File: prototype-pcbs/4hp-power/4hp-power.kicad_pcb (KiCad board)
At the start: 2 copper layers, 17.8 x 109.2 mm, 208 parts, among them J1 IDC Header 2x8

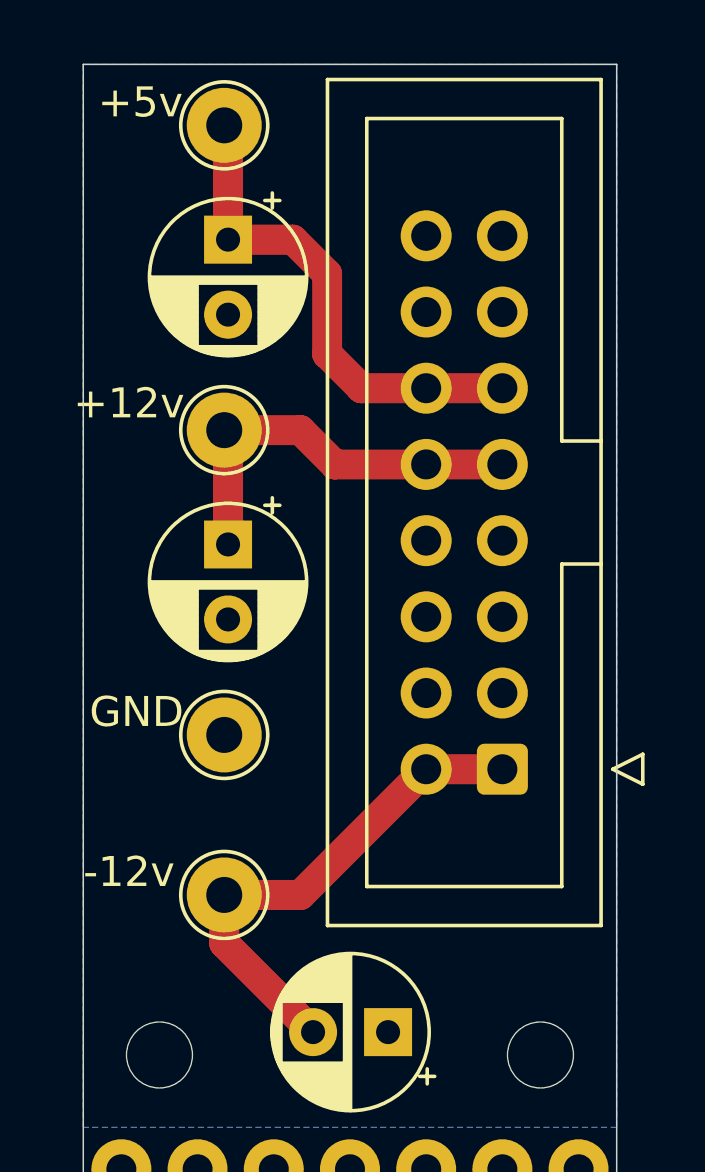
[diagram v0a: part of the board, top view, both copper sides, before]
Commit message: prototype-pcbs: added revision 2.1 for PCBs with Eurorack PSU connector.
gerber's silkscreen was missing the voltage references in the solder
points.
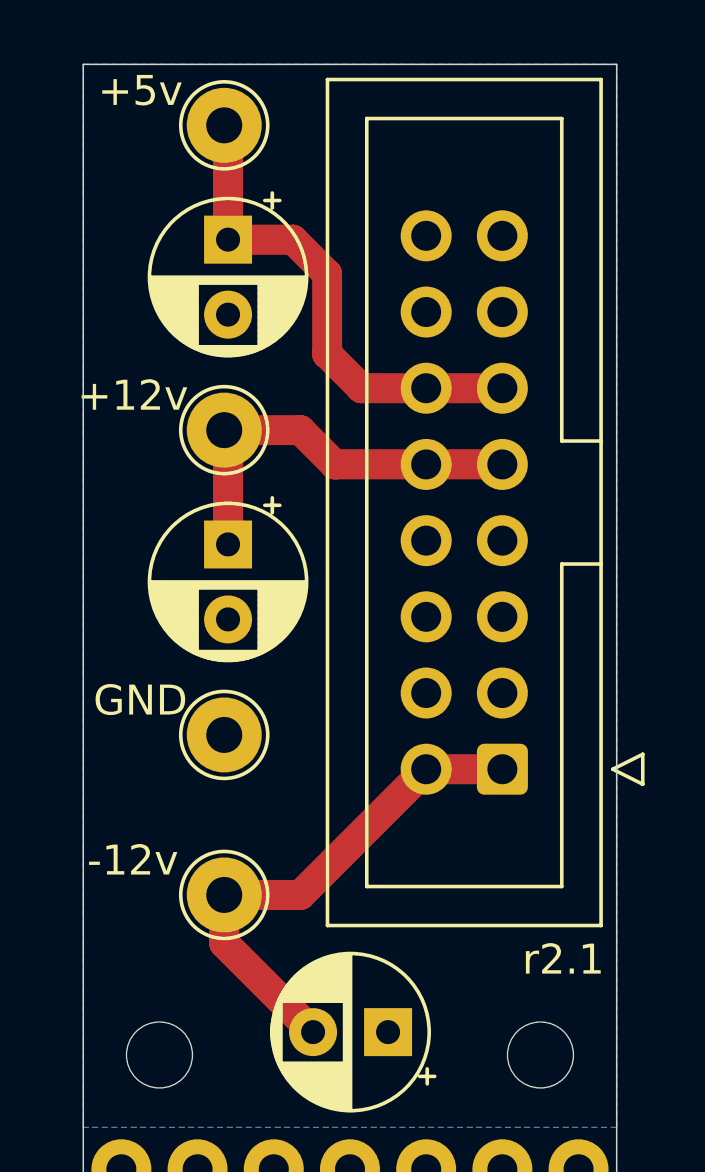
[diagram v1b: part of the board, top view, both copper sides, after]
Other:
- board text added: "r2.1"
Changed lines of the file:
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@@
   (general
     (thickness 1.6)
-    (drawings 7)
+    (drawings 8)
     (tracks 20)
     (zones 0)
@@
   (title_block
     (title "Eurorack prototype 4HP with power")
-    (date 2022-01-09)
-    (rev 2.0)
+    (date 2022-01-23)
+    (rev 2.1)
   )
   (layers
@@
       (psa4output false)
       (plotreference true)
-      (plotvalue false)
+      (plotvalue true)
       (plotinvisibletext false)
       (padsonsilk false)
@@
       (effects (font (size 1 1) (thickness 0.15)))
     )
-    (fp_text value -12v (at -0.762 3.175 180) (layer F.SilkS)
+    (fp_text value -12v (at -1.143 3.048 180) (layer F.SilkS)
       (effects (font (size 1 1) (thickness 0.15)))
     )
@@
       (effects (font (size 1 1) (thickness 0.15)))
     )
-    (fp_text value GND (at -0.762 2.921 180) (layer F.SilkS)
+    (fp_text value GND (at -1.143 2.794 180) (layer F.SilkS)
       (effects (font (size 1 1) (thickness 0.15)))
     )
@@
       (effects (font (size 1 1) (thickness 0.15)))
     )
-    (fp_text value +12v (at -0.889 3.175 180) (layer F.SilkS)
+    (fp_text value +12v (at -1.143 3.048 180) (layer F.SilkS)
       (effects (font (size 1 1) (thickness 0.15)))
     )
@@
       (effects (font (size 1 1) (thickness 0.15)))
     )
-    (fp_text value +5v (at -0.762 2.794 180) (layer F.SilkS)
+    (fp_text value +5v (at -1.143 2.794 180) (layer F.SilkS)
       (effects (font (size 1 1) (thickness 0.15)))
     )
@@
     (pad 3 thru_hole circle (at 0 2.54 180) (size 1.7 1.7) (drill 1) (layers *.Cu *.Mask)
       (net 1 GND))
-    (pad 1 thru_hole roundrect (at 0 0 180) (size 1.7 1.7) (drill 1) (layers *.Cu *.Mask) (roundrect_rratio 0.147059)
+    (pad 1 thru_hole roundrect (at 0 0 180) (size 1.7 1.7) (drill 1) (layers *.Cu *.Mask) (roundrect_rratio 0.1470588235294118)
       (net 4 -12V))
     (model ${KISYS3DMOD}/Connector_IDC.3dshapes/IDC-Header_2x08_P2.54mm_Vertical.wrl
@@
     (pad 1 thru_hole circle (at 0 0) (size 2 2) (drill 1) (layers *.Cu *.Mask))
   )
+  (gr_text r2.1 (at 165.862 67.945) (layer F.SilkS)
+    (effects (font (size 1 1) (thickness 0.15)))
+  )
   (dimension 109.22 (width 0.15) (layer Dwgs.User)

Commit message: prototype-pcbs: 4hp-power: upgrade to kicad 6
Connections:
- J1 pad 13: (no net) -> unconnected-(J1-Pad13)
- J1 pad 14: (no net) -> unconnected-(J1-Pad14)
- J1 pad 15: (no net) -> unconnected-(J1-Pad15)
- J1 pad 16: (no net) -> unconnected-(J1-Pad16)
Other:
- net class Default removed

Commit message: prototype-pcbs: 4hp-power: remove unconnected nets
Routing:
- net -12V: track 18.1 -> 16.8 mm
